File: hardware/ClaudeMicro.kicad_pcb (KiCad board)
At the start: 4 copper layers, 90 x 90 mm, 98 parts, among them J1 USB-C_SMD-TYPE-C-31-M-12_1, J2 SWD, SW1 CONN-SMD_HOTPLUGPAKAGE__C9900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, SW10 CONN-SMD_HOTPLUGPAKAGE__C9900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, SW11 CONN-SMD_HOTPLUGPAKAGE__C9900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, SW12 CONN-SMD_HOTPLUGPAKAGE__C9900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, SW13 SW-SMD_4P-L5.1-W5.1-P3.70-LS6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, SW14 CONN-SMD_HOTPLUGPAKAGE__C9900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, SW2 CONN-SMD_HOTPLUGPAKAGE__C9900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, SW3 CONN-SMD_HOTPLUGPAKAGE__C9900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, SW4 CONN-SMD_HOTPLUGPAKAGE__C9900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, SW5 CONN-SMD_HOTPLUGPAKAGE__C9900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, SW6 CONN-SMD_HOTPLUGPAKAGE__C9900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, SW7 CONN-SMD_HOTPLUGPAKAGE__C9900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, SW8 CONN-SMD_HOTPLUGPAKAGE__C9900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, SW9 CONN-SMD_HOTPLUGPAKAGE__C9900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, U1 LQFN-56_L7.0-W7.0-P0.4-EP, U2 SOIC-8_L5.3-W5.3-P1.27-LS8.0-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, U3 SOT-223-3_L6.5-W3.4-P2.30-LS7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, U4 SOT-23-5_L3.0-W1.7-P0.95-LS2.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, U6 SOT-23-6_L2.9-W1.6-P0.95-LS2.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, Y1 CRYSTAL-SMD_4P-L3.2-W2.5-BL

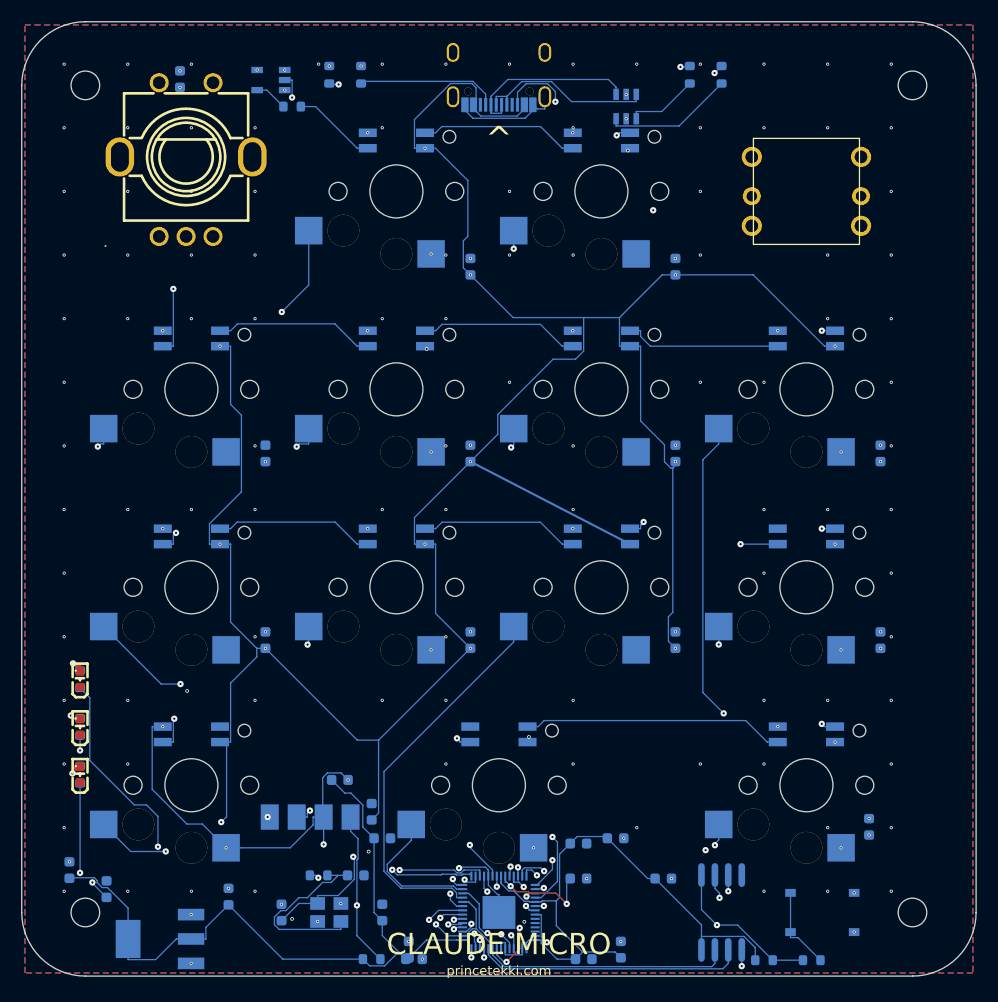
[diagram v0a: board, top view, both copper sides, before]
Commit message: fix: clear DRC errors, adjust silkscreen, regenerate fab package
- Add GND stitching via at (55.605, 88.624) connecting orphan B.Cu
  island carrying C12 pad 2 (decoupling cap ground was floating)
- Remove 9 redundant vias drilled on top of ENC1/JS1/J1 PTH pad holes
- Convert 26 zero-annular-ring switch alignment posts (SW1-SW14) to NPTH
- Silkscreen text repositioned; clears silk_edge_clearance warning
- Schematic resaved by KiCad 10 (format normalization, sch_revision V0.1)
- Regenerate gerbers, drills, CPL from DRC-clean board (0 errors)
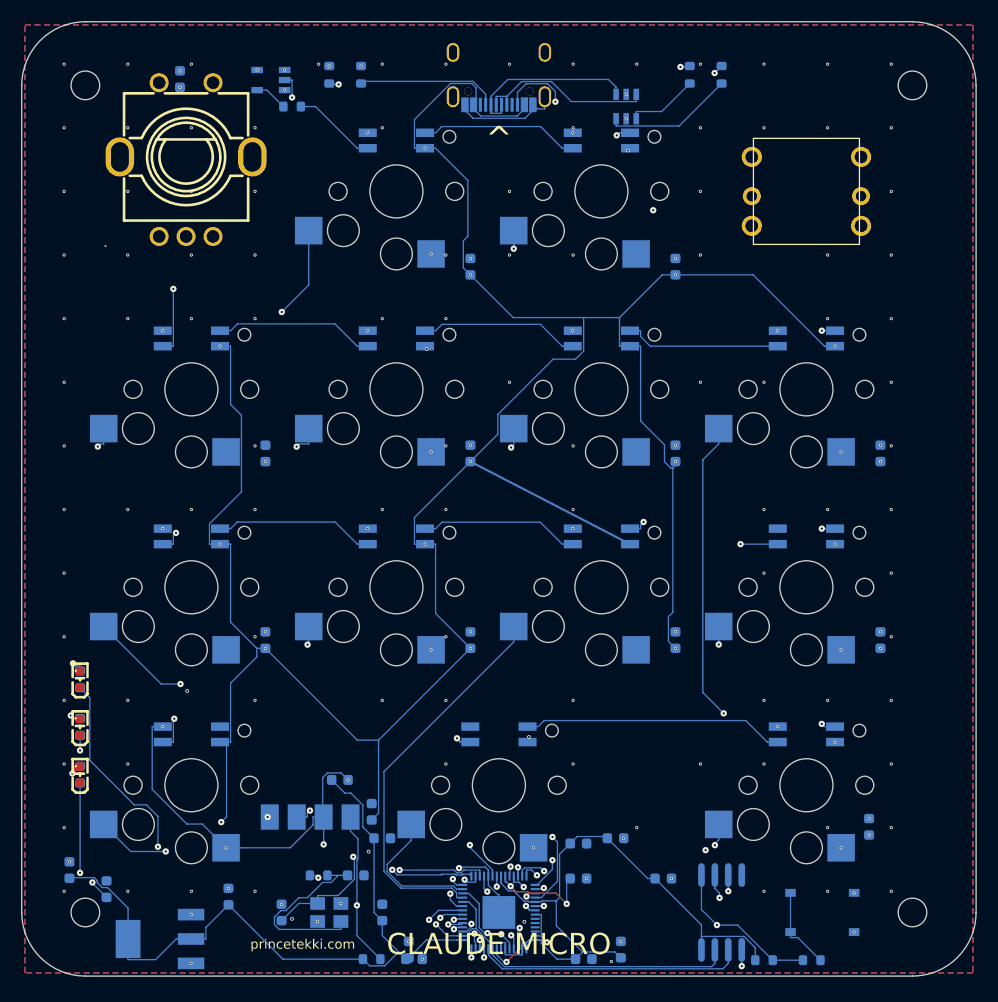
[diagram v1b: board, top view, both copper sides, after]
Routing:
- net GND: vias 167 -> 159
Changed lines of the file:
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@@
 			(layers "*.Cu" "*.Mask")
 		)
-		(pad "" thru_hole circle
+		(pad "" np_thru_hole circle
 			(at -2.5 -1.1)
 			(size 3 3)
 			(drill 3)
-			(layers "*.Cu" "*.Mask")
-			(remove_unused_layers no)
+			(layers "*.Mask")
 		)
 		(pad "" np_thru_hole circle
@@
 			(layers "*.Cu" "*.Mask")
 		)
-		(pad "" thru_hole circle
+		(pad "" np_thru_hole circle
 			(at 2.5 1.1)
 			(size 3 3)
 			(drill 3)
-			(layers "*.Cu" "*.Mask")
-			(remove_unused_layers no)
+			(layers "*.Mask")
 		)
 		(pad "" np_thru_hole circle
@@
 			(layers "*.Cu" "*.Mask")
 		)
-		(pad "" thru_hole circle
+		(pad "" np_thru_hole circle
 			(at -2.5 -1.1)
 			(size 3 3)
 			(drill 3)
-			(layers "*.Cu" "*.Mask")
-			(remove_unused_layers no)
+			(layers "*.Mask")
 		)
 		(pad "" np_thru_hole circle
@@
 			(layers "*.Cu" "*.Mask")
 		)
-		(pad "" thru_hole circle
+		(pad "" np_thru_hole circle
 			(at 2.5 1.1)
 			(size 3 3)
 			(drill 3)
-			(layers "*.Cu" "*.Mask")
-			(remove_unused_layers no)
+			(layers "*.Mask")
 		)
 		(pad "" np_thru_hole circle
@@
 			(layers "*.Cu" "*.Mask")
 		)
-		(pad "" thru_hole circle
+		(pad "" np_thru_hole circle
 			(at -2.5 -1.1)
 			(size 3 3)
 			(drill 3)
-			(layers "*.Cu" "*.Mask")
-			(remove_unused_layers no)
+			(layers "*.Mask")
 		)
 		(pad "" np_thru_hole circle
@@
 			(layers "*.Cu" "*.Mask")
 		)
-		(pad "" thru_hole circle
+		(pad "" np_thru_hole circle
 			(at 2.5 1.1)
 			(size 3 3)
 			(drill 3)
-			(layers "*.Cu" "*.Mask")
-			(remove_unused_layers no)
+			(layers "*.Mask")
 		)
 		(pad "" np_thru_hole circle
@@
 			(layers "*.Cu" "*.Mask")
 		)
-		(pad "" thru_hole circle
+		(pad "" np_thru_hole circle
 			(at -2.5 -1.1)
 			(size 3 3)
 			(drill 3)
-			(layers "*.Cu" "*.Mask")
-			(remove_unused_layers no)
+			(layers "*.Mask")
 		)
 		(pad "" np_thru_hole circle
@@
 			(layers "*.Cu" "*.Mask")
 		)
-		(pad "" thru_hole circle
+		(pad "" np_thru_hole circle
 			(at 2.5 1.1)
 			(size 3 3)
 			(drill 3)
-			(layers "*.Cu" "*.Mask")
-			(remove_unused_layers no)
+			(layers "*.Mask")
 		)
 		(pad "" np_thru_hole circle
@@
 			(layers "*.Cu" "*.Mask")
 		)
-		(pad "" thru_hole circle
+		(pad "" np_thru_hole circle
 			(at -2.5 -1.1)
 			(size 3 3)
 			(drill 3)
-			(layers "*.Cu" "*.Mask")
-			(remove_unused_layers no)
+			(layers "*.Mask")
 		)
 		(pad "" np_thru_hole circle
@@
 			(layers "*.Cu" "*.Mask")
 		)
-		(pad "" thru_hole circle
+		(pad "" np_thru_hole circle
 			(at 2.5 1.1)
 			(size 3 3)
 			(drill 3)
-			(layers "*.Cu" "*.Mask")
-			(remove_unused_layers no)
+			(layers "*.Mask")
 		)
 		(pad "" np_thru_hole circle
@@
 			(layers "*.Cu" "*.Mask")
 		)
-		(pad "" thru_hole circle
+		(pad "" np_thru_hole circle
 			(at -2.5 -1.1)
 			(size 3 3)
 			(drill 3)
-			(layers "*.Cu" "*.Mask")
-			(remove_unused_layers no)
+			(layers "*.Mask")
 		)
 		(pad "" np_thru_hole circle
@@
 			(layers "*.Cu" "*.Mask")
 		)
-		(pad "" thru_hole circle
+		(pad "" np_thru_hole circle
 			(at 2.5 1.1)
 			(size 3 3)
 			(drill 3)
-			(layers "*.Cu" "*.Mask")
-			(remove_unused_layers no)
+			(layers "*.Mask")
 		)
 		(pad "" np_thru_hole circle
@@
 			(layers "*.Cu" "*.Mask")
 		)
-		(pad "" thru_hole circle
+		(pad "" np_thru_hole circle
 			(at -2.5 -1.1)
 			(size 3 3)
 			(drill 3)
-			(layers "*.Cu" "*.Mask")
-			(remove_unused_layers no)
+			(layers "*.Mask")
 		)
 		(pad "" np_thru_hole circle
@@
 			(layers "*.Cu" "*.Mask")
 		)
-		(pad "" thru_hole circle
+		(pad "" np_thru_hole circle
 			(at 2.5 1.1)
 			(size 3 3)
 			(drill 3)
-			(layers "*.Cu" "*.Mask")
-			(remove_unused_layers no)
+			(layers "*.Mask")
 		)
 		(pad "" np_thru_hole circle
@@
 			(layers "*.Cu" "*.Mask")
 		)
-		(pad "" thru_hole circle
+		(pad "" np_thru_hole circle
 			(at -2.5 -1.1)
 			(size 3 3)
 			(drill 3)
-			(layers "*.Cu" "*.Mask")
-			(remove_unused_layers no)
+			(layers "*.Mask")
 		)
 		(pad "" np_thru_hole circle
@@
 			(layers "*.Cu" "*.Mask")
 		)
-		(pad "" thru_hole circle
+		(pad "" np_thru_hole circle
 			(at 2.5 1.1)
 			(size 3 3)
 			(drill 3)
-			(layers "*.Cu" "*.Mask")
-			(remove_unused_layers no)
+			(layers "*.Mask")
 		)
 		(pad "" np_thru_hole circle
@@
 			(layers "*.Cu" "*.Mask")
 		)
-		(pad "" thru_hole circle
+		(pad "" np_thru_hole circle
 			(at -2.5 -1.1)
 			(size 3 3)
 			(drill 3)
-			(layers "*.Cu" "*.Mask")
-			(remove_unused_layers no)
+			(layers "*.Mask")
 		)
 		(pad "" np_thru_hole circle
@@
 			(layers "*.Cu" "*.Mask")
 		)
-		(pad "" thru_hole circle
+		(pad "" np_thru_hole circle
 			(at 2.5 1.1)
 			(size 3 3)
 			(drill 3)
-			(layers "*.Cu" "*.Mask")
-			(remove_unused_layers no)
+			(layers "*.Mask")
 		)
 		(pad "" np_thru_hole circle
@@
 			(layers "*.Cu" "*.Mask")
 		)
-		(pad "" thru_hole circle
+		(pad "" np_thru_hole circle
 			(at -2.5 -1.1)
 			(size 3 3)
 			(drill 3)
-			(layers "*.Cu" "*.Mask")
-			(remove_unused_layers no)
+			(layers "*.Mask")
 		)
 		(pad "" np_thru_hole circle
@@
 			(layers "*.Cu" "*.Mask")
 		)
-		(pad "" thru_hole circle
+		(pad "" np_thru_hole circle
 			(at 2.5 1.1)
 			(size 3 3)
 			(drill 3)
-			(layers "*.Cu" "*.Mask")
-			(remove_unused_layers no)
+			(layers "*.Mask")
 		)
 		(pad "" np_thru_hole circle
@@
 			(layers "*.Cu" "*.Mask")
 		)
-		(pad "" thru_hole circle
+		(pad "" np_thru_hole circle
 			(at -2.5 -1.1)
 			(size 3 3)
 			(drill 3)
-			(layers "*.Cu" "*.Mask")
-			(remove_unused_layers no)
+			(layers "*.Mask")
 		)
 		(pad "" np_thru_hole circle
@@
 			(layers "*.Cu" "*.Mask")
 		)
-		(pad "" thru_hole circle
+		(pad "" np_thru_hole circle
 			(at 2.5 1.1)
 			(size 3 3)
 			(drill 3)
-			(layers "*.Cu" "*.Mask")
-			(remove_unused_layers no)
+			(layers "*.Mask")
 		)
 		(pad "" np_thru_hole circle
@@
 			(layers "*.Cu" "*.Mask")
 		)
-		(pad "" thru_hole circle
+		(pad "" np_thru_hole circle
 			(at -2.5 -1.1)
 			(size 3 3)
 			(drill 3)
-			(layers "*.Cu" "*.Mask")
-			(remove_unused_layers no)
+			(layers "*.Mask")
 		)
 		(pad "" np_thru_hole circle
@@
 			(layers "*.Cu" "*.Mask")
 		)
-		(pad "" thru_hole circle
+		(pad "" np_thru_hole circle
 			(at 2.5 1.1)
 			(size 3 3)
 			(drill 3)
-			(layers "*.Cu" "*.Mask")
-			(remove_unused_layers no)
+			(layers "*.Mask")
 		)
 		(pad "" np_thru_hole circle
@@
 			(layers "*.Cu" "*.Mask")
 		)
-		(pad "" thru_hole circle
+		(pad "" np_thru_hole circle
 			(at -2.5 -1.1)
 			(size 3 3)
 			(drill 3)
-			(layers "*.Cu" "*.Mask")
-			(remove_unused_layers no)
+			(layers "*.Mask")
 		)
 		(pad "" np_thru_hole circle
@@
 			(layers "*.Cu" "*.Mask")
 		)
-		(pad "" thru_hole circle
+		(pad "" np_thru_hole circle
 			(at 2.5 1.1)
 			(size 3 3)
 			(drill 3)
-			(layers "*.Cu" "*.Mask")
-			(remove_unused_layers no)
+			(layers "*.Mask")
 		)
 		(pad "" np_thru_hole circle
@@
 	)
 	(gr_text "princetekki.com"
-		(at 45 89.5 0)
+		(at 26.5 87 0)
 		(layer "F.SilkS")
 		(effects
@@
 	)
 	(via
-		(at 21.75 12.75)
-		(size 0.3)
-		(drill 0.15)
-		(layers "F.Cu" "B.Cu")
-		(net "GND")
-	)
-	(via
 		(at 64 34)
 		(size 0.3)
@@
 	)
 	(via
-		(at 9.25 12.75)
-		(size 0.3)
-		(drill 0.15)
-		(layers "F.Cu" "B.Cu")
-		(net "GND")
-	)
-	(via
 		(at 40 70)
 		(size 0.3)
@@
 	)
 	(via
-		(at 40.67 2.895)
+		(at 55.605 88.624)
 		(size 0.3)
 		(drill 0.15)
@@
 	)
 	(via
-		(at 15.5 20.25)
-		(size 0.3)
-		(drill 0.15)
-		(layers "F.Cu" "B.Cu")
-		(net "GND")
-	)
-	(via
 		(at 34 28)
 		(size 0.3)
@@
 	)
 	(via
-		(at 18.04 5.75)
-		(size 0.3)
-		(drill 0.15)
-		(layers "F.Cu" "B.Cu")
-		(net "GND")
-	)
-	(via
 		(at 22 10)
 		(size 0.3)
@@
 	)
 	(via
-		(at 49.33 2.895)
-		(size 0.3)
-		(drill 0.15)
-		(layers "F.Cu" "B.Cu")
-		(net "GND")
-	)
-	(via
 		(at 64 4)
 		(size 0.3)
@@
 	)
 	(via
-		(at 79.15 19.25)
-		(size 0.3)
-		(drill 0.15)
-		(layers "F.Cu" "B.Cu")
-		(net "GND")
-	)
-	(via
 		(at 4 40)
 		(size 0.3)
@@
 	)
 	(via
-		(at 40.67 7.075)
-		(size 0.3)
-		(drill 0.15)
-		(layers "F.Cu" "B.Cu")
-		(net "GND")
-	)
-	(via
 		(at 61.275 80.8)
 		(size 0.3)
 		(drill 0.15)
-		(layers "F.Cu" "B.Cu")
-		(net "GND")
-	)
-	(via
-		(at 49.33 7.075)
-		(size 0.3)
-		(drill 0.15)
